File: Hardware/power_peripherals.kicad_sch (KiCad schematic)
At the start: 37 parts, among them J2 JST_2mm_LiPo, J3 Qwiic_RA, J7 Conn_01x12, J8 Conn_01x12, J9 microSD_Friction, U5 LM66200, U6 RT9080-3.3, U7 MCP73831, U8 MAX17048, U9 RT9080-3.3

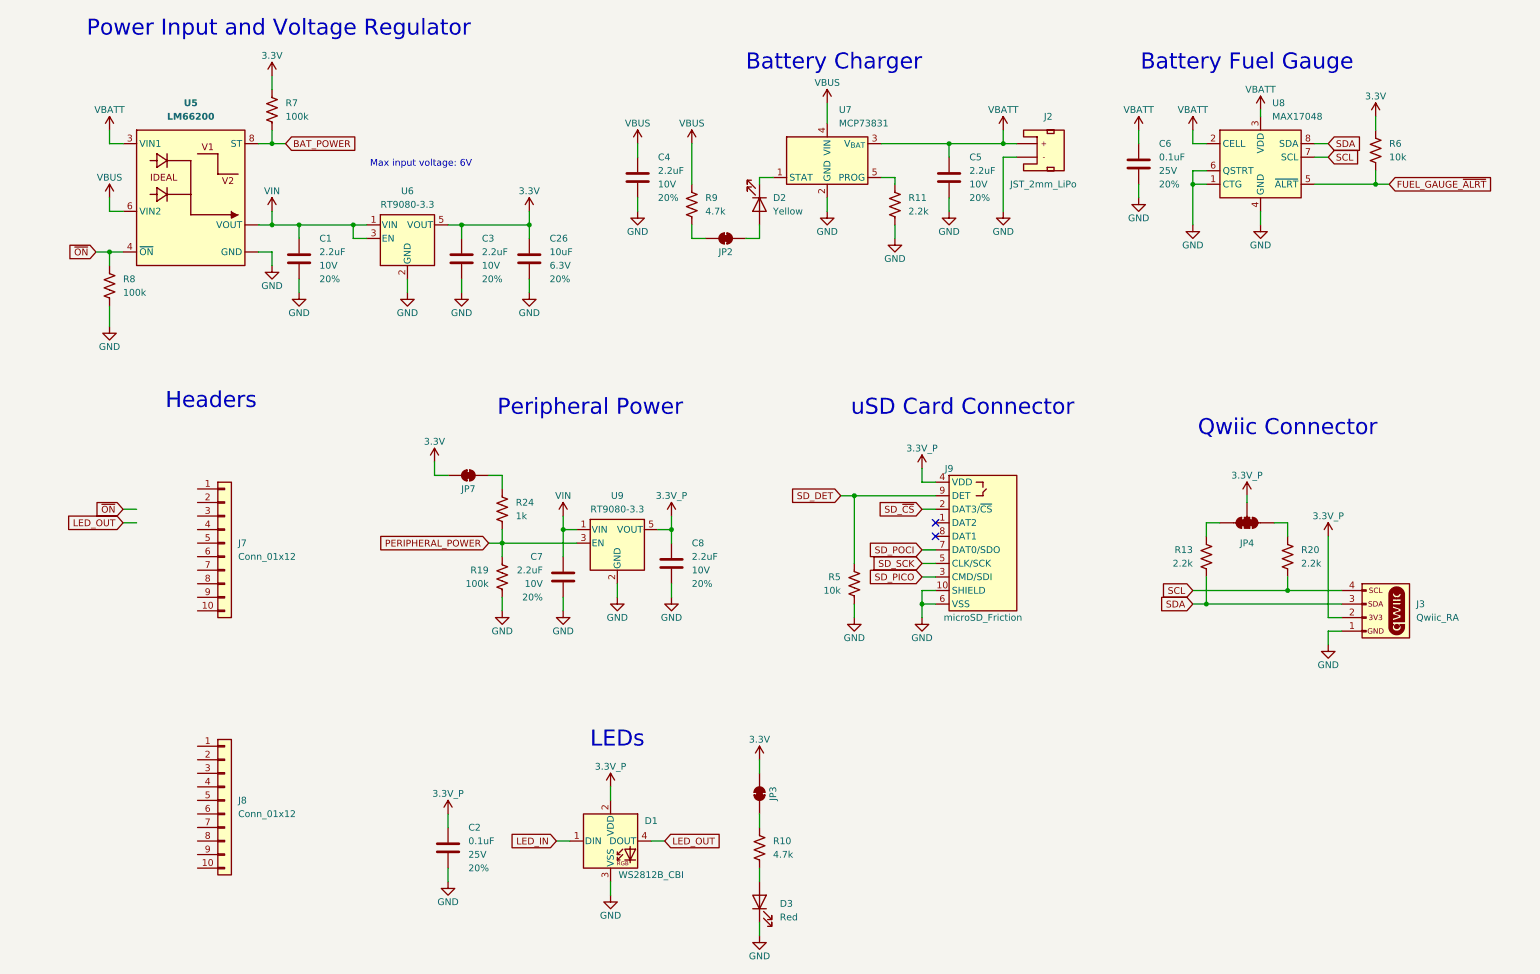
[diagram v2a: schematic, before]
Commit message: Finish connections and routing
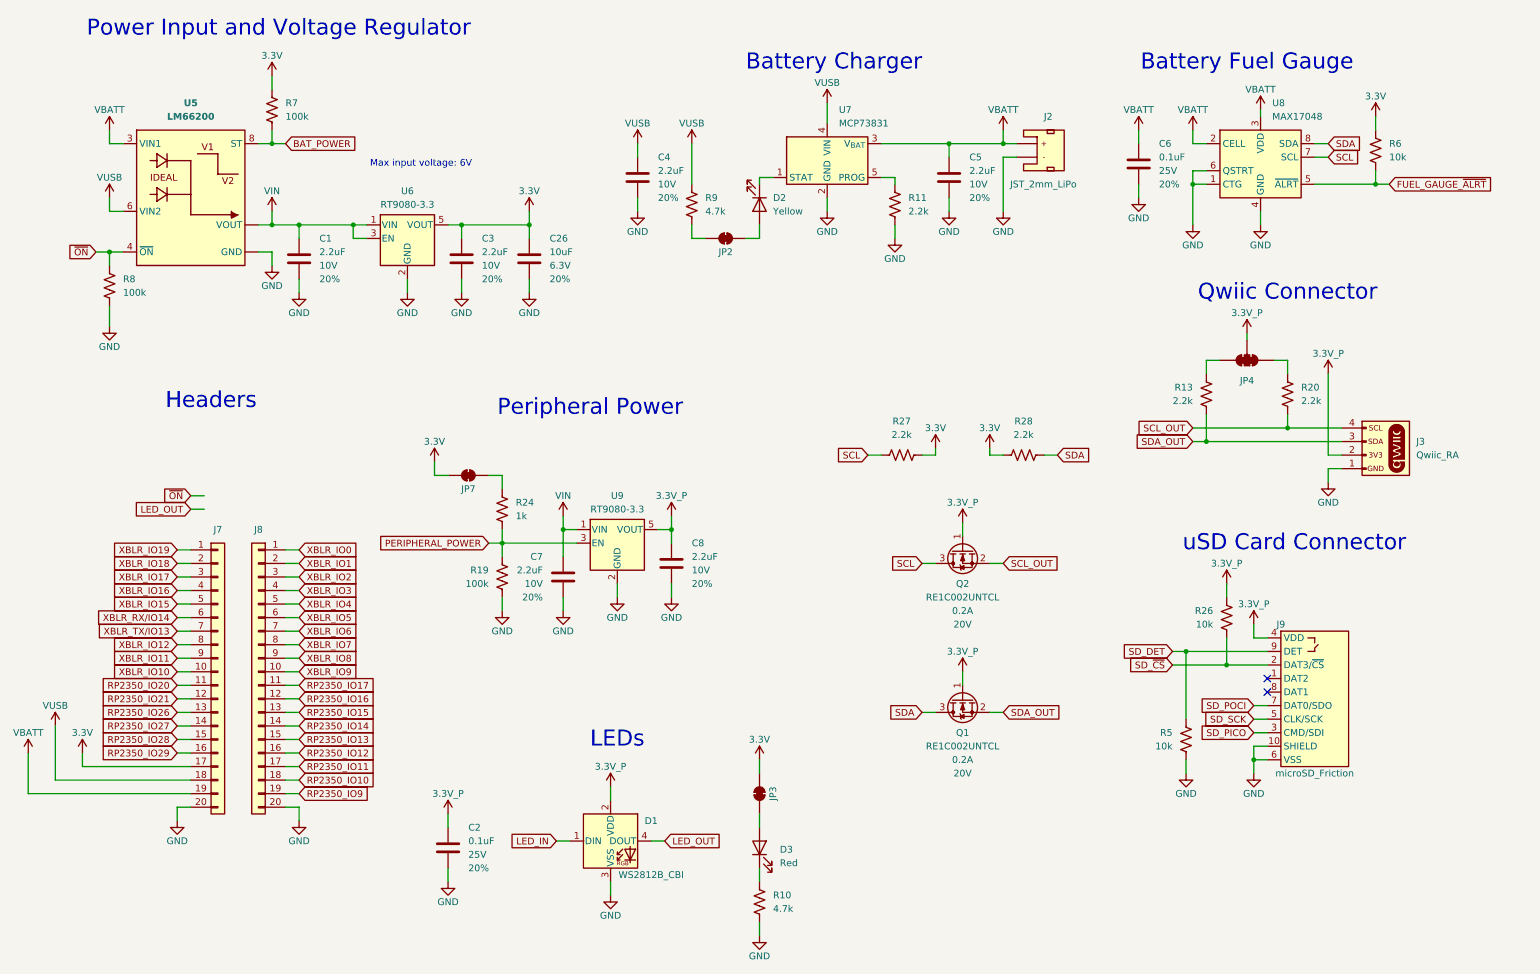
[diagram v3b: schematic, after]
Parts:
- removed J7, J8: Conn_01x12, SparkFun-Connector:1x10, symbol SparkFun-Connector:Conn_01x10
- added J7, J8: Conn_01x12, SparkFun-Connector:1x20, symbol SparkFun-Connector:Conn_01x20
- added Q1, Q2: RE1C002UNTCL, SparkFun-Semiconductor-Standard:SC-89 SOT-490, symbol SparkFun-DiscreteSemi:Q_NMOS_0.2A_20V
- added R26: 10k, SparkFun-Resistor:R_0603_1608Metric, symbol SparkFun-Resistor:10k_0603
- added R27, R28: 2.2k, SparkFun-Resistor:R_0603_1608Metric, symbol SparkFun-Resistor:2.2k_0603
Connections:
- net 3.3V: now also J7.17 (Pin_17), R27.1, R28.1
- net 3.3V_P: now also Q1.1 (G), Q2.1 (G), R26.1
- net GND: now also R10.2, J7.20 (Pin_20), J8.20 (Pin_20); no longer D3.1 (K)
- net SCL: now also Q2.3 (D), R27.2; no longer J3.4 (Pin_4), R20.2
- net SDA: now also Q1.3 (D), R28.2; no longer J3.3 (Pin_3), R13.2
- net SD_~{CS}: now also R26.2
- net VBATT: now also J7.19 (Pin_19)
- net at D3.2 (A): now also JP3.1 (A); no longer R10.2
- net at R10.1: now also D3.1 (K); no longer JP3.1 (A)
- net VBUS renamed VUSB
- net VUSB: now also J7.18 (Pin_18)
- new net RP2350_IO10: J8.18 (Pin_18)
- new net RP2350_IO11: J8.17 (Pin_17)
- new net RP2350_IO12: J8.16 (Pin_16)
- new net RP2350_IO13: J8.15 (Pin_15)
- new net RP2350_IO14: J8.14 (Pin_14)
- new net RP2350_IO15: J8.13 (Pin_13)
- new net RP2350_IO16: J8.12 (Pin_12)
- new net RP2350_IO17: J8.11 (Pin_11)
- new net RP2350_IO20: J7.11 (Pin_11)
- new net RP2350_IO21: J7.12 (Pin_12)
- new net RP2350_IO26: J7.13 (Pin_13)
- new net RP2350_IO27: J7.14 (Pin_14)
- new net RP2350_IO28: J7.15 (Pin_15)
- new net RP2350_IO29: J7.16 (Pin_16)
- new net RP2350_IO9: J8.19 (Pin_19)
- new net SCL_OUT: J3.4 (Pin_4), Q2.2 (S), R20.2
- new net SDA_OUT: J3.3 (Pin_3), Q1.2 (S), R13.2
- new net XBLR_IO0: J8.1 (Pin_1)
- new net XBLR_IO1: J8.2 (Pin_2)
- new net XBLR_IO10: J7.10 (Pin_10)
- new net XBLR_IO11: J7.9 (Pin_9)
- new net XBLR_IO12: J7.8 (Pin_8)
- new net XBLR_IO15: J7.5 (Pin_5)
- new net XBLR_IO16: J7.4 (Pin_4)
- new net XBLR_IO17: J7.3 (Pin_3)
- new net XBLR_IO18: J7.2 (Pin_2)
- new net XBLR_IO19: J7.1 (Pin_1)
- new net XBLR_IO2: J8.3 (Pin_3)
- new net XBLR_IO3: J8.4 (Pin_4)
- new net XBLR_IO4: J8.5 (Pin_5)
- new net XBLR_IO5: J8.6 (Pin_6)
- new net XBLR_IO6: J8.7 (Pin_7)
- new net XBLR_IO7: J8.8 (Pin_8)
- new net XBLR_IO8: J8.9 (Pin_9)
- new net XBLR_IO9: J8.10 (Pin_10)
- new net XBLR_RX/IO14: J7.6 (Pin_6)
- new net XBLR_TX/IO13: J7.7 (Pin_7)
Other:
- moved on the sheet: J3, J9, JP4, R13, R20, R5

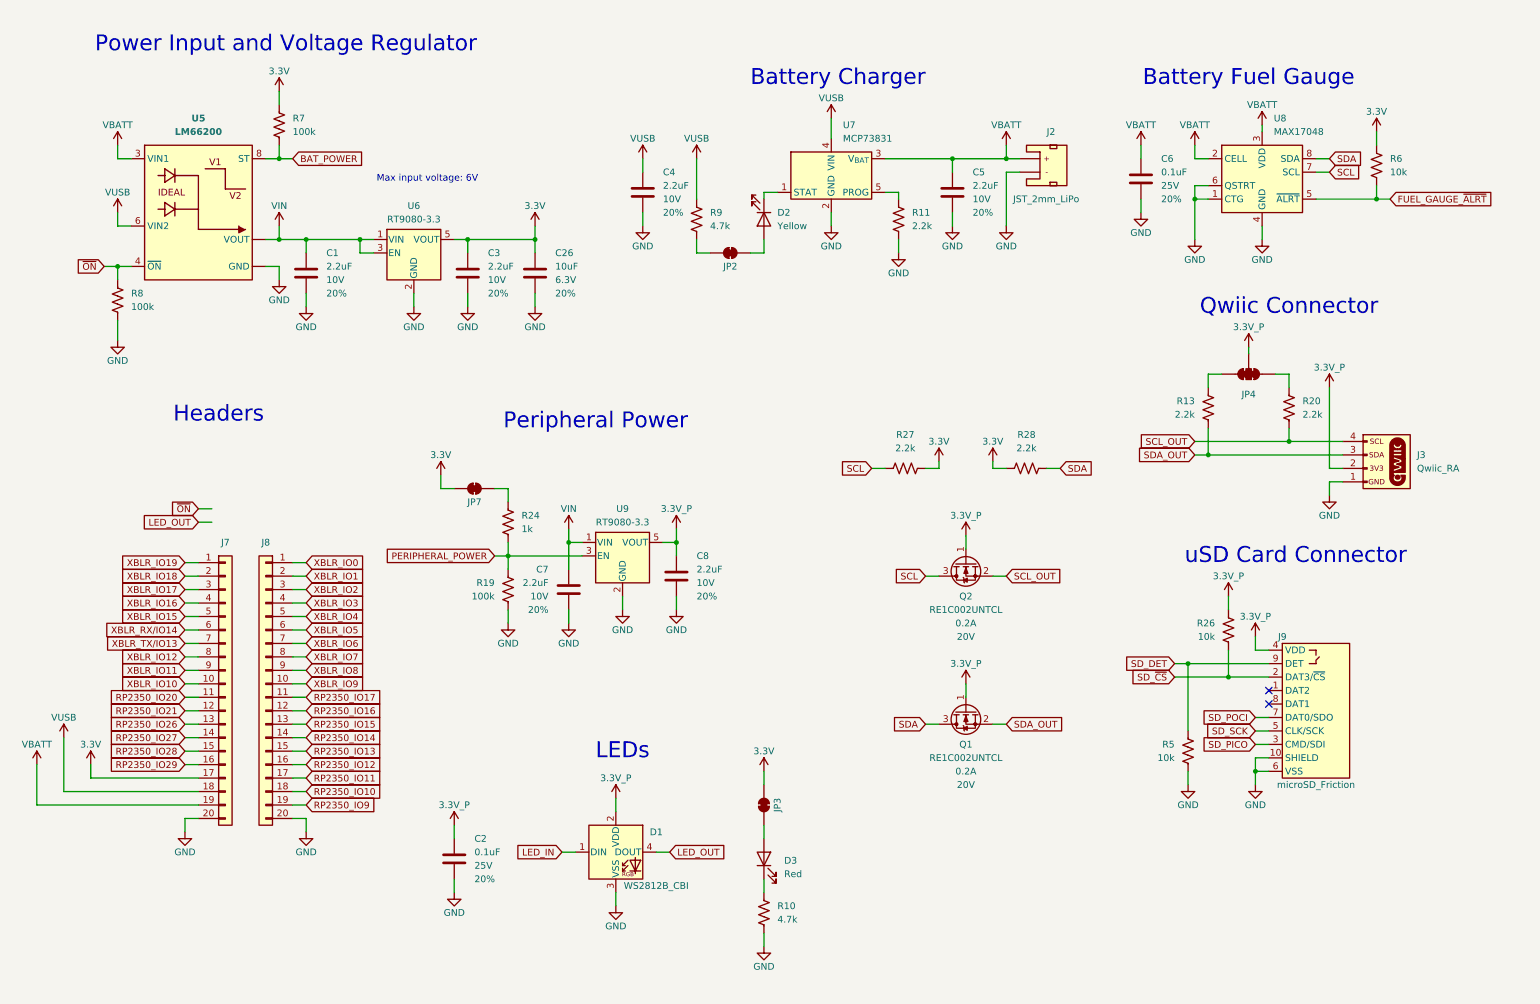
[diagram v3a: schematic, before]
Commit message: Clean up schematic
Add lines between regions
Add instruction text to all jumpers
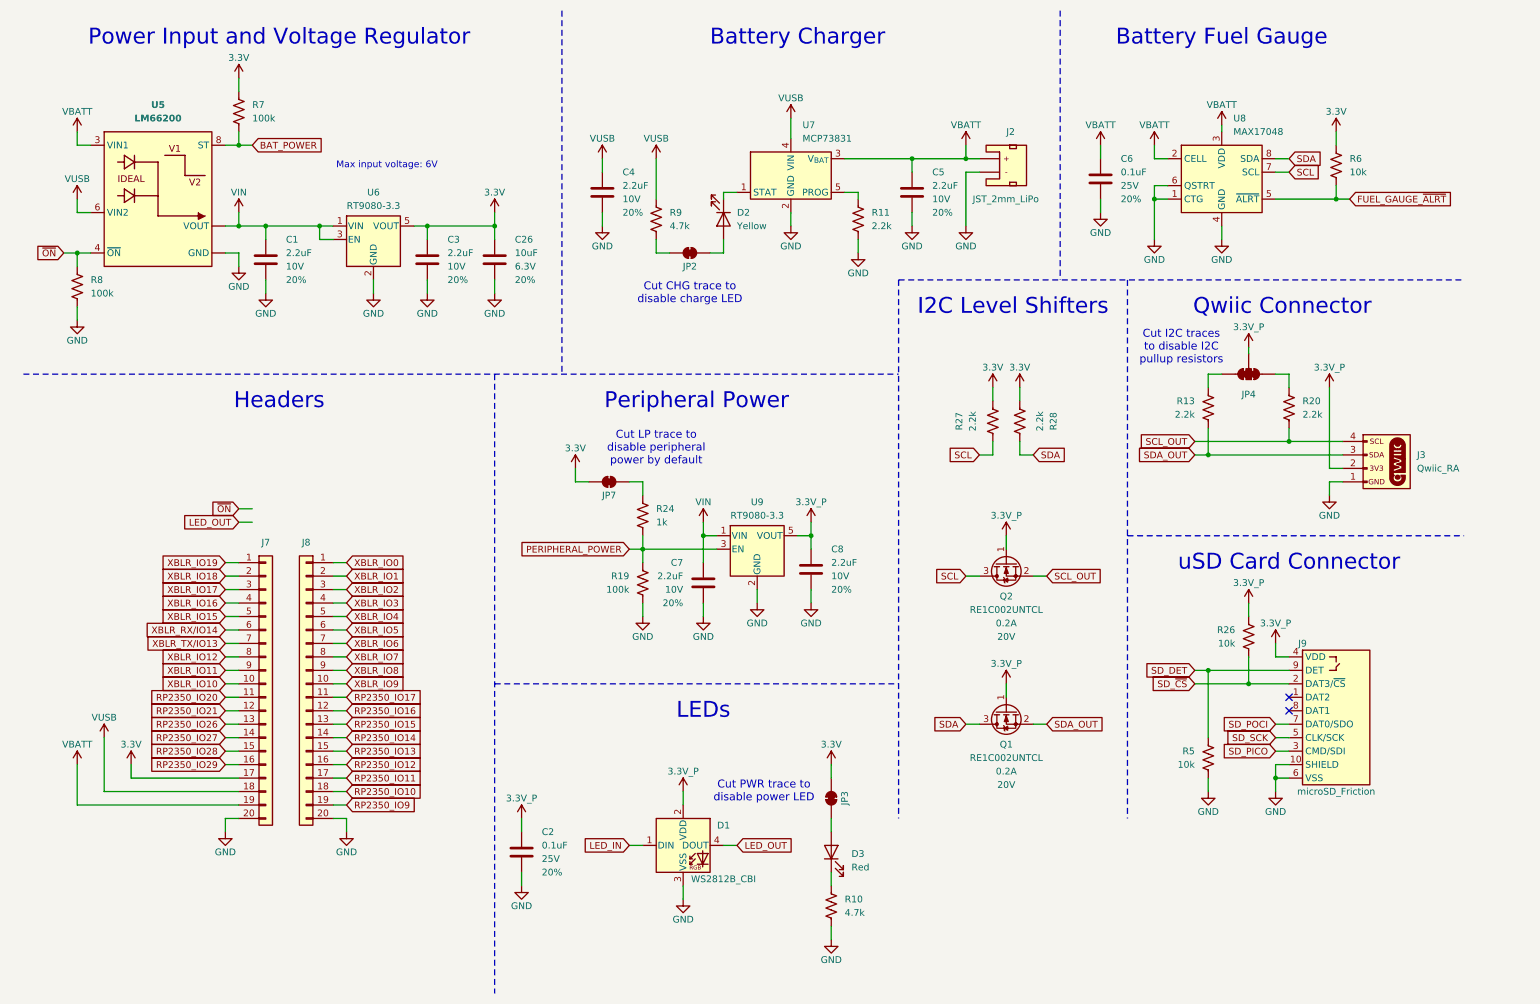
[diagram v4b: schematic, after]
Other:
- note added: "Cut CHG trace to disable charge LED"
- note added: "Cut I2C traces to disable I2C pullup resistors"
- note added: "Cut LP trace to disable peripheral power by default"
- note added: "Cut PWR trace to disable power LED"
- note added: "I2C Level Shifters"
- moved on the sheet: C1, C2, C26, C3, C4, C5, C6, C7, C8, D1, D2, D3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

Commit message: v02 Schematic Updates
Bump version number to v02
Fix RP2350, APS6404L, and 12MHz crystal to use proper KiCad symbols and footprints instead of imported from Eagle
Change schematic to use 2x Ledger sheets
Change Qwiic connector to power from 3.3V
Change user button and RGB LED to small mount versions
Split headers into XBLR and IoT Node specific regions
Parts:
- removed J7, J8: Conn_01x12, SparkFun-Connector:1x20, symbol SparkFun-Connector:Conn_01x20
- removed Q1, Q2: RE1C002UNTCL, SparkFun-Semiconductor-Standard:SC-89 SOT-490, symbol SparkFun-DiscreteSemi:Q_NMOS_0.2A_20V
- removed R27, R28: 2.2k, SparkFun-Resistor:R_0603_1608Metric, symbol SparkFun-Resistor:2.2k_0603
- added J10, J11, J7, J8: Conn_01x10, SparkFun-Connector:1x10, symbol SparkFun-Connector:Conn_01x10
- D1: footprint SparkFun-LED:WS2812B-CBI -> SparkFun-LED:WS2812-2020; symbol SparkFun-LED:WS2812B_CBI -> SparkFun-LED:WS2812B_2020; PROD_ID LED-20286 -> DIO-15591
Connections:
- net SCL_OUT is gone; now on net SCL: J3.4 (Pin_4), R20.2
- net SDA_OUT is gone; now on net SDA: J3.3 (Pin_3), R13.2
- net 3.3V: now also J3.2 (Pin_2), JP4.2 (C), J10.7 (Pin_7)
- net 3.3V_P: now also D1.4 (VDD); no longer D1.2 (VDD), J3.2 (Pin_2), JP4.2 (C)
- net GND: now also D1.2 (VSS), J10.10 (Pin_10), J11.10 (Pin_10); no longer D1.3 (VSS)
- net LED_IN: now also D1.3 (DIN); no longer D1.1 (DIN)
- net LED_OUT: now also D1.1 (DOUT); no longer D1.4 (DOUT)
- net RP2350_IO10: now also J11.8 (Pin_8)
- net RP2350_IO11: now also J11.7 (Pin_7)
- net RP2350_IO12: now also J11.6 (Pin_6)
- net RP2350_IO13: now also J11.5 (Pin_5)
- net RP2350_IO14: now also J11.4 (Pin_4)
- net RP2350_IO15: now also J11.3 (Pin_3)
- net RP2350_IO16: now also J11.2 (Pin_2)
- net RP2350_IO17: now also J11.1 (Pin_1)
- net RP2350_IO20: now also J10.1 (Pin_1)
- net RP2350_IO21: now also J10.2 (Pin_2)
- net RP2350_IO26: now also J10.3 (Pin_3)
- net RP2350_IO27: now also J10.4 (Pin_4)
- net RP2350_IO28: now also J10.5 (Pin_5)
- net RP2350_IO29: now also J10.6 (Pin_6)
- net RP2350_IO9: now also J11.9 (Pin_9)
- net VBATT: now also J10.9 (Pin_9)
- net VUSB: now also J10.8 (Pin_8)
- net XBLR_IO0: now also J8.1 (Pin_1)
- net XBLR_IO1: now also J8.2 (Pin_2)
- net XBLR_IO10: now also J7.10 (Pin_10)
- net XBLR_IO11: now also J7.9 (Pin_9)
- net XBLR_IO12: now also J7.8 (Pin_8)
- net XBLR_IO15: now also J7.5 (Pin_5)
- net XBLR_IO16: now also J7.4 (Pin_4)
- net XBLR_IO17: now also J7.3 (Pin_3)
- net XBLR_IO18: now also J7.2 (Pin_2)
- net XBLR_IO19: now also J7.1 (Pin_1)
- net XBLR_IO2: now also J8.3 (Pin_3)
- net XBLR_IO3: now also J8.4 (Pin_4)
- net XBLR_IO4: now also J8.5 (Pin_5)
- net XBLR_IO5: now also J8.6 (Pin_6)
- net XBLR_IO6: now also J8.7 (Pin_7)
- net XBLR_IO7: now also J8.8 (Pin_8)
- net XBLR_IO8: now also J8.9 (Pin_9)
- net XBLR_IO9: now also J8.10 (Pin_10)
- net XBLR_RX/IO14: now also J7.6 (Pin_6)
- net XBLR_TX/IO13: now also J7.7 (Pin_7)
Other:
- note added: "IoT Node Headers"
- note added: "XBLR Headers"
- note removed: "Headers"
- note removed: "I2C Level Shifters"
- company: (none) -> SparkFun
- title: (none) -> SparkFun IoT Node - LoRaWAN
- moved on the sheet: C1, C2, C26, C3, C4, C5, C6, C7, C8, D1, D2, D3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
